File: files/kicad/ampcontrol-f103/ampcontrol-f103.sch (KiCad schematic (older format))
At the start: 65 parts, among them J1 SP, J10 Buttons, J11 Encoder, J12 LCD_CTRL, J13 I2C, J14 I2C, J15 I2C, J16 SPI, J17 SPI, J18 SPI, J2 MUTE_STBY, J3 UART1, J4 USB, J5 UART2, J6 UART3, J7 RC, J8 LCD_DATA, J9 5V, Q1 BSS138, SW1 Reset, U1 MCP602, U2 STM32F103CBTx, U3 AMS1117-3.3, Y1 8MHz, Y2 32768

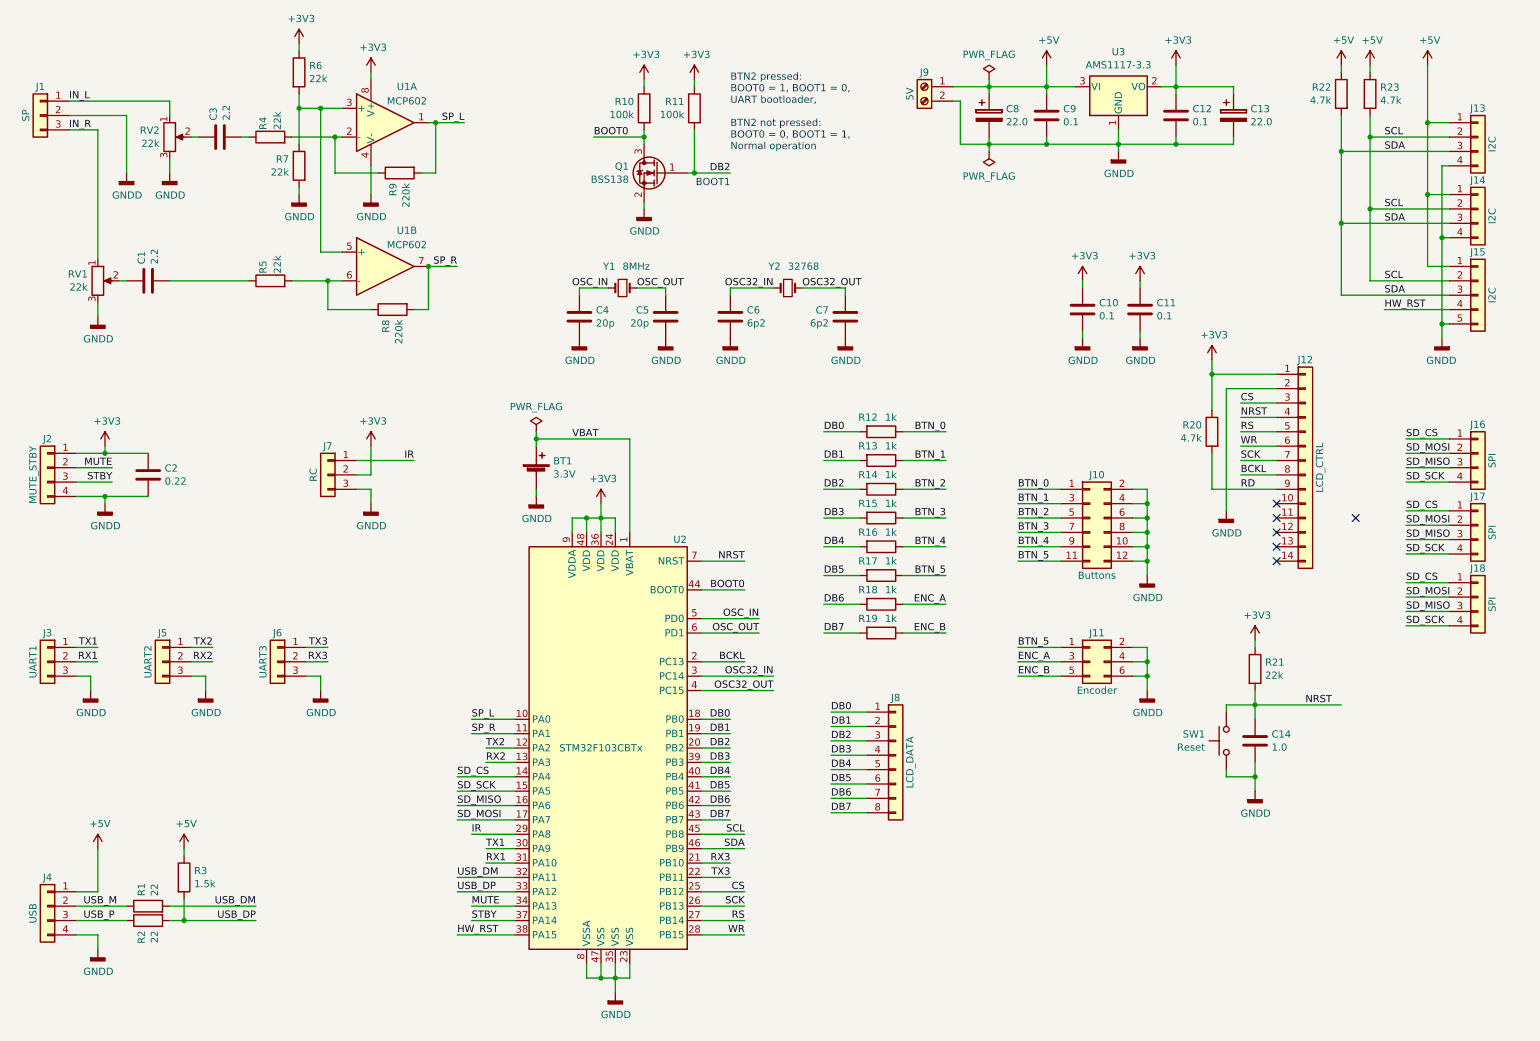
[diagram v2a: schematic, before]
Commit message: Add sockets for arduino-pinout displays
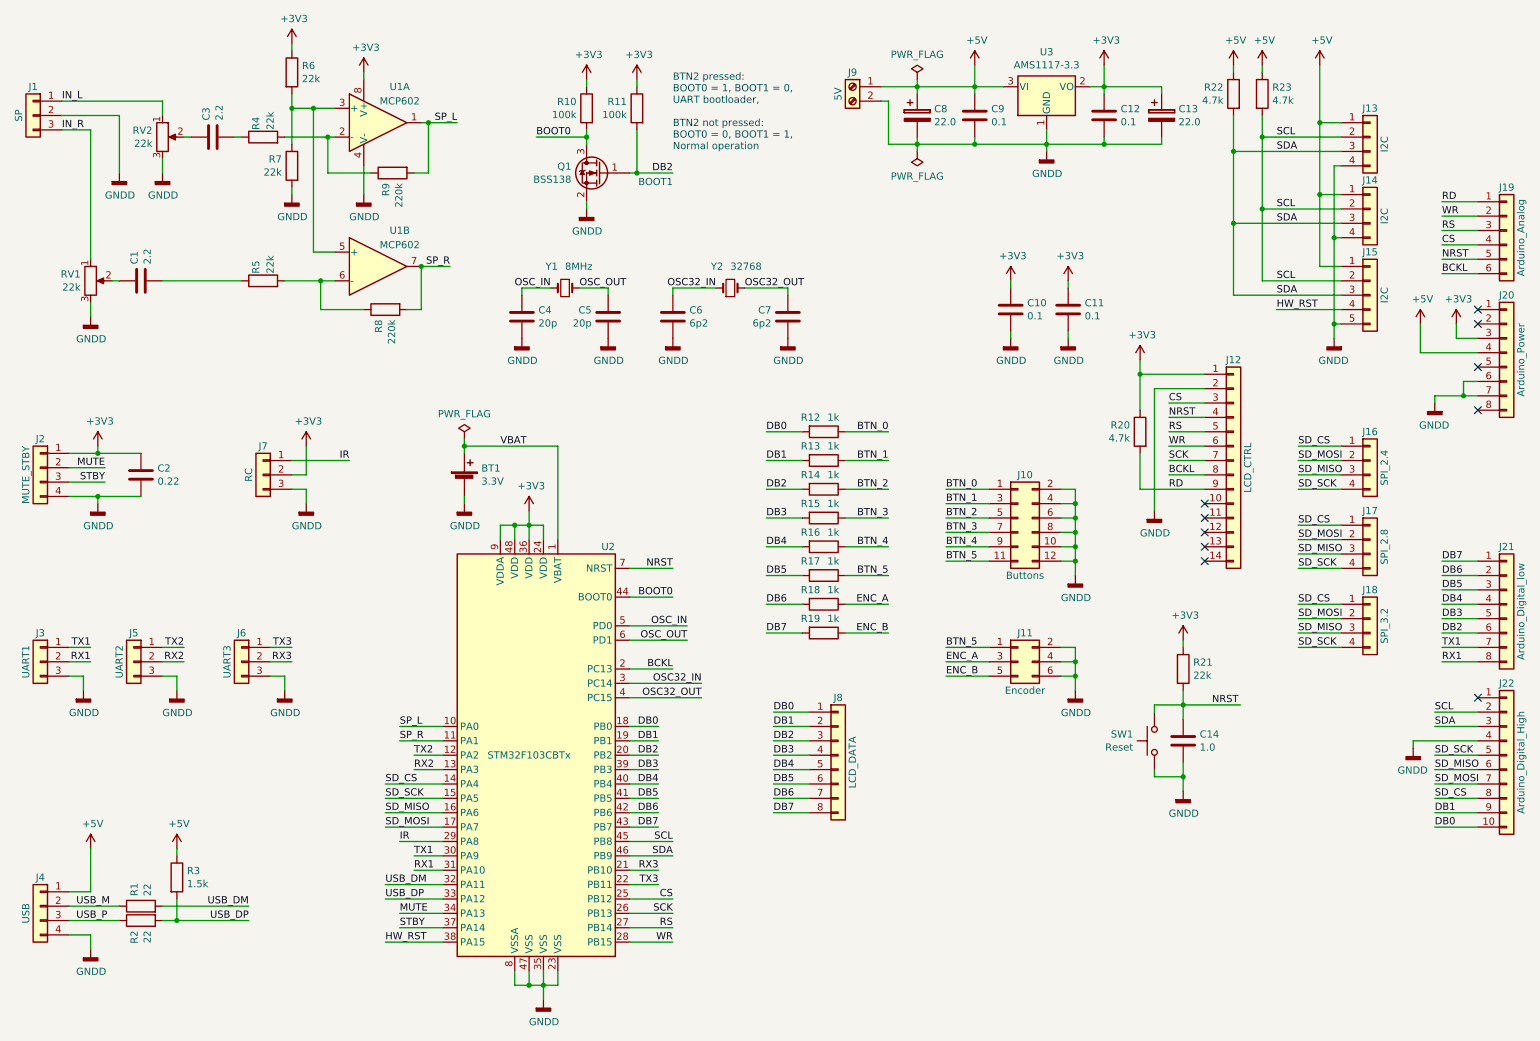
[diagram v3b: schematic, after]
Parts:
- added J19: Arduino_Analog, Connector_PinSocket_2.54mm:PinSocket_1x06_P2.54mm_Vertical, symbol Connector_Generic:Conn_01x06
- added J20: Arduino_Power, Connector_PinSocket_2.54mm:PinSocket_1x08_P2.54mm_Vertical, symbol Connector_Generic:Conn_01x08
- added J21: Arduino_Digital_low, Connector_PinSocket_2.54mm:PinSocket_1x08_P2.54mm_Vertical, symbol Connector_Generic:Conn_01x08
- added J22: Arduino_Digital_High, Connector_PinSocket_2.54mm:PinSocket_1x10_P2.54mm_Vertical, symbol Connector_Generic:Conn_01x10
- J16: value SPI -> SPI_2.4
- J17: value SPI -> SPI_2.8
- J18: value SPI -> SPI_3.2
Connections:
- net +3V3: now also J20.3 (Pin_3)
- net +5V: now also J20.4 (Pin_4)
- net BCKL: now also J19.6 (Pin_6)
- net CS: now also J19.4 (Pin_4)
- net DB0: now also J22.10 (Pin_10)
- net DB1: now also J22.9 (Pin_9)
- net DB2: now also J21.6 (Pin_6)
- net DB3: now also J21.5 (Pin_5)
- net DB4: now also J21.4 (Pin_4)
- net DB5: now also J21.3 (Pin_3)
- net DB6: now also J21.2 (Pin_2)
- net DB7: now also J21.1 (Pin_1)
- net GNDD: now also J20.6 (Pin_6), J20.7 (Pin_7), J22.4 (Pin_4)
- net NRST: now also J19.5 (Pin_5)
- net RD: now also J19.1 (Pin_1)
- net RS: now also J19.3 (Pin_3)
- net RX1: now also J21.8 (Pin_8)
- net SCL: now also J22.2 (Pin_2)
- net SDA: now also J22.3 (Pin_3)
- net SD_CS: now also J22.8 (Pin_8)
- net SD_MISO: now also J22.6 (Pin_6)
- net SD_MOSI: now also J22.7 (Pin_7)
- net SD_SCK: now also J22.5 (Pin_5)
- net TX1: now also J21.7 (Pin_7)
- net WR: now also J19.2 (Pin_2)
- no-connect marks 6 -> 10
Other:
- moved on the sheet: BT1, C1, C10, C11, C12, C13, C14, C2, C3, C4, C5, C6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
